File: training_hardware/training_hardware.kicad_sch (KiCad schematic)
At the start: 0 parts

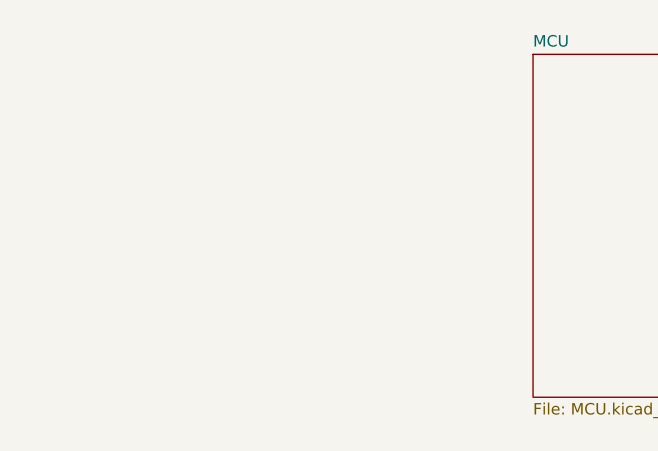
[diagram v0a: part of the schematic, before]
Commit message: Add CAN & Transceiver
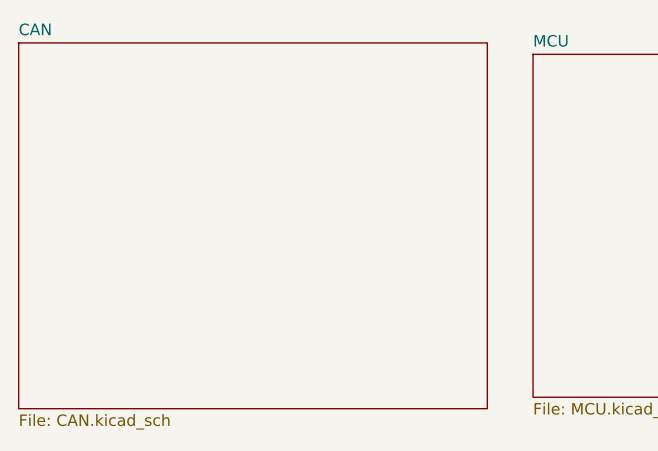
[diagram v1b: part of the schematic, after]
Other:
- added sheet CAN (CAN.kicad_sch)
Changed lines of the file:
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@@
+		)
+	)
+	(sheet
+		(at 69.85 67.31)
+		(size 52.07 40.64)
+		(exclude_from_sim no)
+		(in_bom yes)
+		(on_board yes)
+		(dnp no)
+		(fields_autoplaced yes)
+		(stroke
+			(width 0.1524)
+			(type solid)
+		)
+		(fill
+			(color 0 0 0 0.0000)
+		)
+		(property "Sheetname" "CAN"
+			(at 69.85 66.5984 0)
+			(effects
+				(font
+					(size 1.27 1.27)
+				)
+				(justify left bottom)
+			)
+		)
+		(property "Sheetfile" "CAN.kicad_sch"
+			(at 69.85 108.5346 0)
+			(effects
+				(font
+					(size 1.27 1.27)
+				)
+				(justify left top)
+			)
+		)
+		(instances
+			(project "training_hardware"
+				(path "/13ce2e34-cc5b-4cfe-ac61-3c662d8291c3"
+					(page "4")
+				)
+			)
 		)
 	)

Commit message: Finish Schematic
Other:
- sheet CAN ports: added RXD, STBY, TXD; removed none
- sheet MCU ports: added CRX1, CTX1, STBY; removed none
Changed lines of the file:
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@@
 	(generator_version "9.0")
 	(paper "A4")
+	(wire
+		(pts
+			(xy 121.92 88.9) (xy 127 88.9)
+		)
+		(stroke
+			(width 0)
+			(type default)
+		)
+	)
+	(wire
+		(pts
+			(xy 121.92 78.74) (xy 127 78.74)
+		)
+		(stroke
+			(width 0)
+			(type default)
+		)
+	)
+	(wire
+		(pts
+			(xy 121.92 83.82) (xy 127 83.82)
+		)
+		(stroke
+			(width 0)
+			(type default)
+		)
+	)
 	(sheet
 		(at 193.04 68.58)
@@
 			)
 		)
+		(pin "CTX1" output
+			(at 127 78.74 180)
+			(effects
+				(font
+					(size 1.27 1.27)
+				)
+				(justify left)
+			)
+		)
+		(pin "CRX1" input
+			(at 127 83.82 180)
+			(effects
+				(font
+					(size 1.27 1.27)
+				)
+				(justify left)
+			)
+		)
+		(pin "STBY" output
+			(at 127 88.9 180)
+			(effects
+				(font
+					(size 1.27 1.27)
+				)
+				(justify left)
+			)
+		)
 		(instances
 			(project "training_hardware"
@@
 			)
 		)
+		(pin "RXD" output
+			(at 121.92 83.82 0)
+			(effects
+				(font
+					(size 1.27 1.27)
+				)
+				(justify right)
+			)
+		)
+		(pin "STBY" input
+			(at 121.92 88.9 0)
+			(effects
+				(font
+					(size 1.27 1.27)
+				)
+				(justify right)
+			)
+		)
+		(pin "TXD" input
+			(at 121.92 78.74 0)
+			(effects
+				(font
+					(size 1.27 1.27)
+				)
+				(justify right)
+			)
+		)
